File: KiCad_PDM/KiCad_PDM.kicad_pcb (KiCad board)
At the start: 4 copper layers, 100 x 175 mm, 317 parts, among them J1 Conn_02x16_Top_Bottom, J2 6437288-1, J3 T66145145-1500, U1 74HC27D, U10 INA180A3IDBVR, U11 2N7002, U12 NSG2000, U13 OSP80N03T, U14 2N7002, U15 INA180A3IDBVR, U16 2N7002, U17 NSG2000, U18 OSP80N03T, U19 2N7002, U2 74HC27D, U20 INA180A3IDBVR, U21 2N7002, U22 NSG2000, U23 OSP80N03T, U24 2N7002, U25 INA180A3IDBVR, U26 2N7002, U27 NSG2000, U28 OSP80N03T, U29 2N7002, U3 74HC27D, U30 INA180A3IDBVR, U31 2N7002, U32 NSG2000, U33 OSP80N03T, U34 2N7002, U35 INA180A3IDBVR, U36 2N7002, U37 NSG2000, U38 OSP80N03T, U39 2N7002, U4 74HC27D, U40 INA180A3IDBVR, U41 2N7002, U42 NSG2000, U43 OSP80N03T, U44 2N7002, U45 INA180A3IDBVR, U46 2N7002, U47 NSG2000, U48 OSP80N03T, U49 2N7002, U5 KF33BDT-TR, U50 INA180A3IDBVR, U51 2N7002, U52 NSG2000, U53 OSP80N03T, U54 2N7002, U55 INA180A3IDBVR, U6 2N7002, U7 NSG2000, U8 OSP80N03T, U9 2N7002

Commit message: MK1
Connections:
- J1 pad 1: +3.3V -> Ch8_MCU
- J1 pad 10: Aux5 -> Ch4_MCU
- J1 pad 11: Ch10_MCU -> CS3
- J1 pad 12: CS1 -> unconnected-(J1-Pin_12-Pad12)
- J1 pad 13: CS2 -> Can_Lo
- J1 pad 14: CS3 -> GND
- J1 pad 15: CS4 -> Aux6
- J1 pad 16: GND -> Aux4
- J1 pad 17: CS5 -> +BATT
- J1 pad 18: CS6 -> Aux3
- J1 pad 19: CS7 -> Aux1
- J1 pad 2: Ch3_MCU -> CS8
- J1 pad 20: CS8 -> Aux2
- J1 pad 21: CS9 -> Aux5
- J1 pad 22: CS10 -> CS2
- J1 pad 23: Aux2 -> Can_Hi
- J1 pad 24: Aux3 -> CS5
- J1 pad 25: +BATT -> CS9
- J1 pad 26: Aux4 -> Ch1_MCU
- J1 pad 27: Ch9_MCU -> CS7
- J1 pad 28: Aux1 -> Ch5_MCU
- J1 pad 29: Ch7_MCU -> Ch9_MCU
- J1 pad 3: Ch4_MCU -> CS4
- J1 pad 30: Ch1_MCU -> Ch2_MCU
- J1 pad 31: Ch2_MCU -> CS1
- J1 pad 32: Ch5_MCU -> Ch7_MCU
- J1 pad 4: Ch6_MCU -> +3.3V
- J1 pad 5: Ch8_MCU -> Ch10_MCU
- J1 pad 6: Can_Lo -> Ch3_MCU
- J1 pad 7: Can_Hi -> CS10
- J1 pad 8: unconnected-(J1-Pin_8-Pad8) -> Ch6_MCU
- J1 pad 9: Aux6 -> CS6
- J2 pad 11: SW2 -> Can_Hi
- J2 pad 12: Aux1 -> Aux5
- J2 pad 19: Aux5 -> SW1
- J2 pad 2: Can_Hi -> SW5
- J2 pad 21: unconnected-(J2-Pad21) -> BSPD_In
- J2 pad 24: Aux6 -> unconnected-(J2-Pad24)
- J2 pad 27: SW1 -> SW2
- J2 pad 4: SW5 -> Aux1
- J2 pad 6: BSPD_In -> Aux6
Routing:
- net +3.3V: track 231.0 -> 823.0 mm, vias 0 -> 20
- net GND: track 0.00 -> 133.8 mm, vias 0 -> 743
- net Ch9_MCU: track 3.76 -> 123.8 mm, vias 1 -> 2
- net Ch7_MCU: track 3.75 -> 119.5 mm, vias 1 -> 2
- net Ch10_MCU: track 3.74 -> 116.0 mm
- net Ch8_MCU: track 3.97 -> 108.7 mm
- net CS10: track 1.13 -> 102.3 mm
- net CS9: track 1.20 -> 101.4 mm
- net CS6: track 1.38 -> 101.0 mm
- net CS5: track 1.38 -> 95.6 mm
- net Ch4_MCU: track 2.28 -> 87.8 mm, vias 0 -> 1
- net Can_Hi: track 0.00 -> 83.9 mm
- net Ch1_MCU: track 3.97 -> 87.3 mm
- net Aux5: track 0.00 -> 81.5 mm
- net Aux2: track 0.00 -> 79.9 mm
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- added copper zone on B.Cu, net GND
- added copper zone on F.Cu, net GND
- added copper zone on In1.Cu, net GND
- added copper zone on In2.Cu, net GND

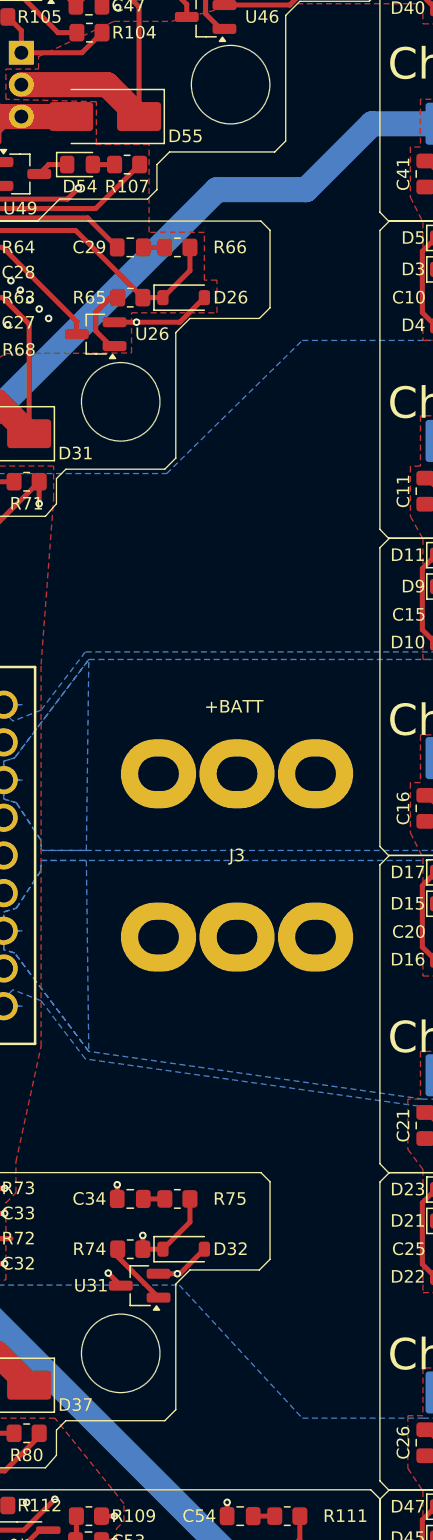
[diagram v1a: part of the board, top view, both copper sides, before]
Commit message: silk screen changes(logos and qr codes)
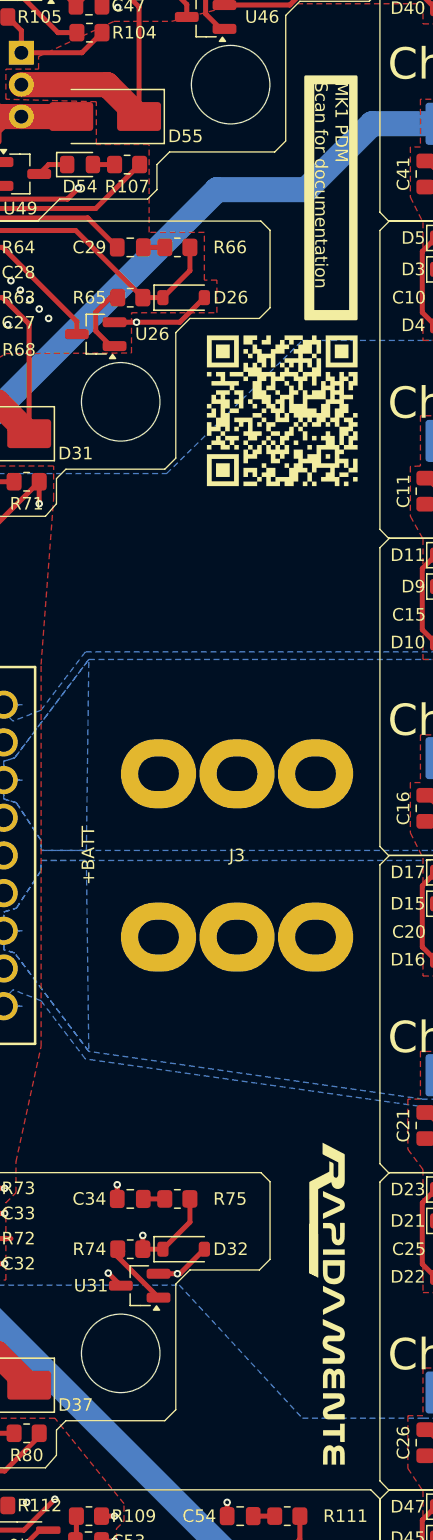
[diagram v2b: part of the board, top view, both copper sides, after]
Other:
- board text added: "@Cubic"
- board text added: "MK1 PDM Scan for documentation"

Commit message: updated design and 3d models
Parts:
- added D13: 1N5819HW-7-F, Diode_SMD:D_SOD-123, B.Cu at (96.3, 77.6)
- added D20: 1N5819HW-7-F, Diode_SMD:D_SOD-123, B.Cu at (96.3, 102.8)
- added D27: 1N5819HW-7-F, Diode_SMD:D_SOD-123, B.Cu at (96.3, 128.1)
- added D34: 1N5819HW-7-F, Diode_SMD:D_SOD-123, B.Cu at (46.3, 52.3)
- added D41: 1N5819HW-7-F, Diode_SMD:D_SOD-123, F.Cu at (42.5, 136.0)
- added D48: 1N5819HW-7-F, Diode_SMD:D_SOD-123, B.Cu at (96.3, 27.1)
- added D55: 1N5819HW-7-F, Diode_SMD:D_SOD-123, B.Cu at (96.3, 153.3)
- added D6: 1N5819HW-7-F, Diode_SMD:D_SOD-123, B.Cu at (96.3, 52.3)
- added D62: 1N5819HW-7-F, Diode_SMD:D_SOD-123, B.Cu at (55.0, 27.1)
- added D69: 1N5819HW-7-F, Diode_SMD:D_SOD-123, B.Cu at (55.0, 153.3)
- renumbered D9 to D10, D10 to D11, D11 to D12, D12 to D14, D13 to D15, D14 to D16, D15 to D17, D16 to D18, D17 to D19, D18 to D21, D19 to D22, D20 to D23, D21 to D24, D22 to D25, D23 to D26, D24 to D28, D25 to D29, D26 to D30, D27 to D31, D28 to D32, D29 to D33, D30 to D35, D31 to D36, D32 to D37, D33 to D38, D34 to D39, D35 to D40, D36 to D42, D37 to D43, D38 to D44, D39 to D45, D40 to D46, D41 to D47, D42 to D49, D43 to D50, D44 to D51, D45 to D52, D46 to D53, D47 to D54, D48 to D56, D49 to D57, D50 to D58, D51 to D59, D52 to D60, D53 to D61, D54 to D63, D55 to D64, D56 to D65, D57 to D66, D58 to D67, D59 to D68, D6 to D7, D60 to D70, D61 to D71, D7 to D8, D8 to D9, H5 to H3, H3 to H4, H4 to H5, R26 to R25, R25 to R26
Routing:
- net Net-(D55-K): track 18.6 -> 22.3 mm
- net Net-(D41-K): track 16.8 -> 19.3 mm
- net Net-(D62-K): track 16.7 -> 18.2 mm
- net Net-(D34-K): track 16.7 -> 18.2 mm
- net Net-(D6-K): track 17.2 -> 18.7 mm
- net Net-(D48-K): track 16.7 -> 18.2 mm
- net Net-(D20-K): track 16.7 -> 18.2 mm
- net Net-(D69-K): track 16.7 -> 18.2 mm
- net Net-(D27-K): track 16.7 -> 18.2 mm
- net Net-(D13-K): track 16.7 -> 18.2 mm
